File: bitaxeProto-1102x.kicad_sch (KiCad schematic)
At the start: 10 parts, among them J1 XT30

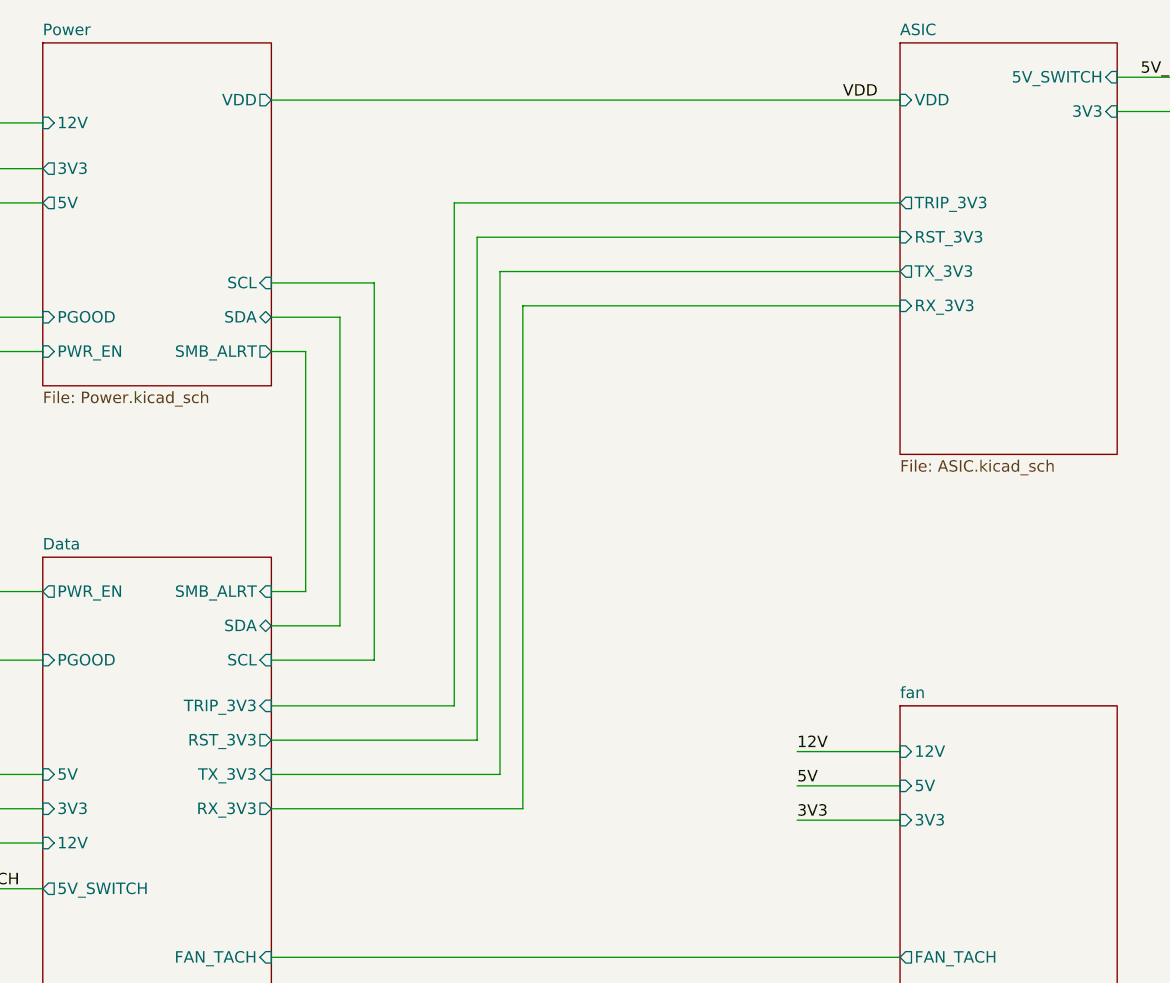
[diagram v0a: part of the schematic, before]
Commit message: switch aux voltage regulators to TPS62933
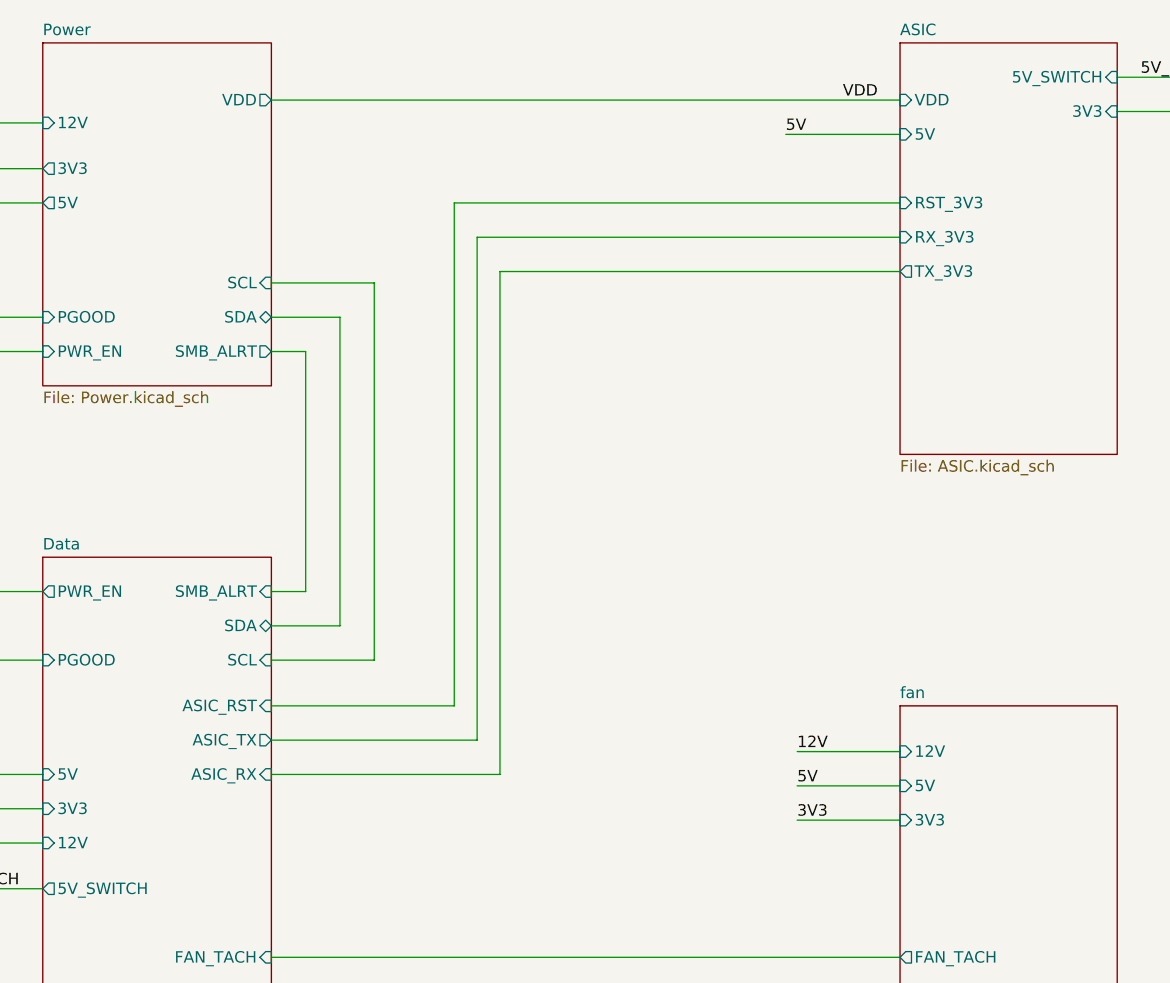
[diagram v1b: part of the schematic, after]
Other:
- sheet ASIC ports: added 5V; removed TRIP_3V3
- sheet Data ports: added ASIC_RST, ASIC_RX, ASIC_TX; removed RST_3V3, RX_3V3, TRIP_3V3, TX_3V3
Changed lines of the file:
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@@
+	(wire
+		(pts
+			(xy 185.42 45.72) (xy 198.12 45.72)
+		)
+		(stroke
+			(width 0)
+			(type default)
+		)
+	)
 	(wire
 		(pts
@@
 	(wire
 		(pts
-			(xy 156.21 64.77) (xy 198.12 64.77)
-		)
-		(stroke
-			(width 0)
-			(type default)
-		)
-	)
-	(wire
-		(pts
 			(xy 132.08 96.52) (xy 132.08 69.85)
 		)
@@
 	(wire
 		(pts
-			(xy 156.21 64.77) (xy 156.21 120.65)
-		)
-		(stroke
-			(width 0)
-			(type default)
-		)
-	)
-	(wire
-		(pts
 			(xy 91.44 66.04) (xy 91.44 104.14)
 		)
@@
 		(pts
 			(xy 96.52 69.85) (xy 96.52 96.52)
-		)
-		(stroke
-			(width 0)
-			(type default)
-		)
-	)
-	(wire
-		(pts
-			(xy 156.21 120.65) (xy 128.27 120.65)
 		)
 		(stroke
@@
 			)
 			(justify right bottom)
+		)
+	)
+	(label "5V"
+		(at 185.42 45.72 0)
+		(effects
+			(font
+				(size 1.27 1.27)
+			)
+			(justify left bottom)
 		)
 	)
@@
 			)
 		)
-		(pin "TX_3V3" input
-			(at 128.27 116.84 0)
-			(effects
-				(font
-					(size 1.27 1.27)
-				)
-				(justify right)
-			)
-		)
-		(pin "RX_3V3" output
-			(at 128.27 120.65 0)
-			(effects
-				(font
-					(size 1.27 1.27)
-				)
-				(justify right)
-			)
-		)
-		(pin "RST_3V3" output
-			(at 128.27 113.03 0)
-			(effects
-				(font
-					(size 1.27 1.27)
-				)
-				(justify right)
-			)
-		)
 		(pin "3V3" input
 			(at 102.87 120.65 180)
@@
 			)
 		)
-		(pin "TRIP_3V3" input
-			(at 128.27 109.22 0)
-			(effects
-				(font
-					(size 1.27 1.27)
-				)
-				(justify right)
-			)
-		)
 		(pin "FAN_PWM" output
 			(at 128.27 140.97 0)
@@
 				)
 				(justify left)
+			)
+		)
+		(pin "ASIC_RST" input
+			(at 128.27 109.22 0)
+			(effects
+				(font
+					(size 1.27 1.27)
+				)
+				(justify right)
+			)
+		)
+		(pin "ASIC_RX" input
+			(at 128.27 116.84 0)
+			(effects
+				(font
+					(size 1.27 1.27)
+				)
+				(justify right)
+			)
+		)
+		(pin "ASIC_TX" output
+			(at 128.27 113.03 0)
+			(effects
+				(font
+					(size 1.27 1.27)
+				)
+				(justify right)
 			)
 		)
@@
 			)
 		)
+		(pin "5V" input
+			(at 198.12 45.72 180)
+			(effects
+				(font
+					(size 1.27 1.27)
+				)
+				(justify left)
+			)
+		)
 		(pin "RST_3V3" input
+			(at 198.12 53.34 180)
+			(effects
+				(font
+					(size 1.27 1.27)
+				)
+				(justify left)
+			)
+		)
+		(pin "RX_3V3" input
 			(at 198.12 57.15 180)
 			(effects
@@
 			(effects
 				(font
-					(size 1.27 1.27)
-				)
-				(justify left)
-			)
-		)
-		(pin "RX_3V3" input
-			(at 198.12 64.77 180)
-			(effects
-				(font
-					(size 1.27 1.27)
-				)
-				(justify left)
-			)
-		)
-		(pin "TRIP_3V3" output
-			(at 198.12 53.34 180)
-			(effects
-				(font
